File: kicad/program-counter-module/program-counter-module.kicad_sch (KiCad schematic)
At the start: 33 parts, among them U1 74LS04, U2 74LS245, U3 74LS245, U4 SB1R1Y8G_LED, U5 SB1R1Y8G_LED, U6 74LS161, U7 74LS161, U8 74LS161, U9 74LS161

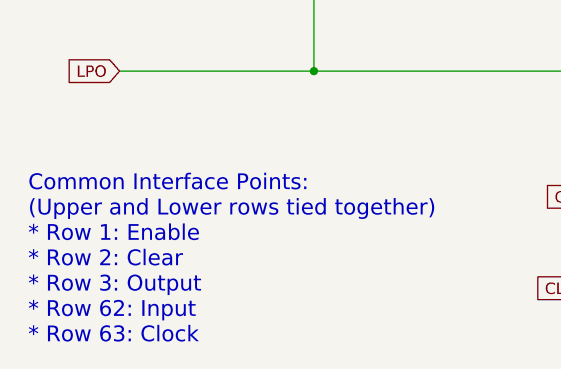
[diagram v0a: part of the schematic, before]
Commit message: Add a reset button to the Power-Up Module
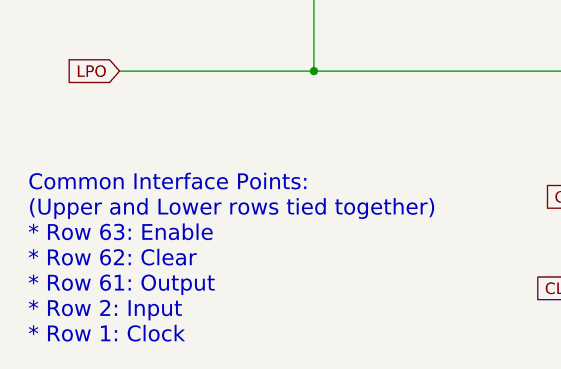
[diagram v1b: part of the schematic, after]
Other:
- note added: "Common Interface Points: (Upper and Lower rows tied together) * Row 63: Enable * Row 62: Clear * Row 61: Output * Row 2: Input * Row 1: Clock"
- note removed: "Common Interface Points: (Upper and Lower rows tied together) * Row 1: Enable * Row 2: Clear * Row 3: Output * Row 62: Input * Row 63: Clock"
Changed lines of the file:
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@@
     (stroke (width 0) (type default) (color 0 0 0 0))
   )
-  (text "Common Interface Points:\n(Upper and Lower rows tied together)\n* Row 1: Enable\n* Row 2: Clear\n* Row 3: Output\n* Row 62: Input\n* Row 63: Clock"
+  (text "Common Interface Points:\n(Upper and Lower rows tied together)\n* Row 63: Enable\n* Row 62: Clear\n* Row 61: Output\n* Row 2: Input\n* Row 1: Clock"
     (at 15.24 201.93 0)
     (effects (font (size 1.75 1.75)) (justify left bottom))
